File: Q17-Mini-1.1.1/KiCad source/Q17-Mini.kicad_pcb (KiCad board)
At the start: 2 copper layers, 95 x 75 mm, 88 parts, among them J1 Input, J2-1 SPK+, J2-2 SPK-, J3-1 V+, J3-2 GND, J3-3 V-, Q1 IRF610, Q10 KSA992, Q11 ZVP2106A, Q12 BD139, Q13 IRF610, Q14 IRF9610, Q15 FQA46N15, Q16 FQA36P15, Q2 KSA992, Q3 KSC1845, Q4 IRF9610, Q5 FQP3P20, Q6 FQP3N30, Q7 KSC1845, Q8 ZVN4206AV, Q9 ZVP2106A, U1 OPA1641, U1' OPA1641

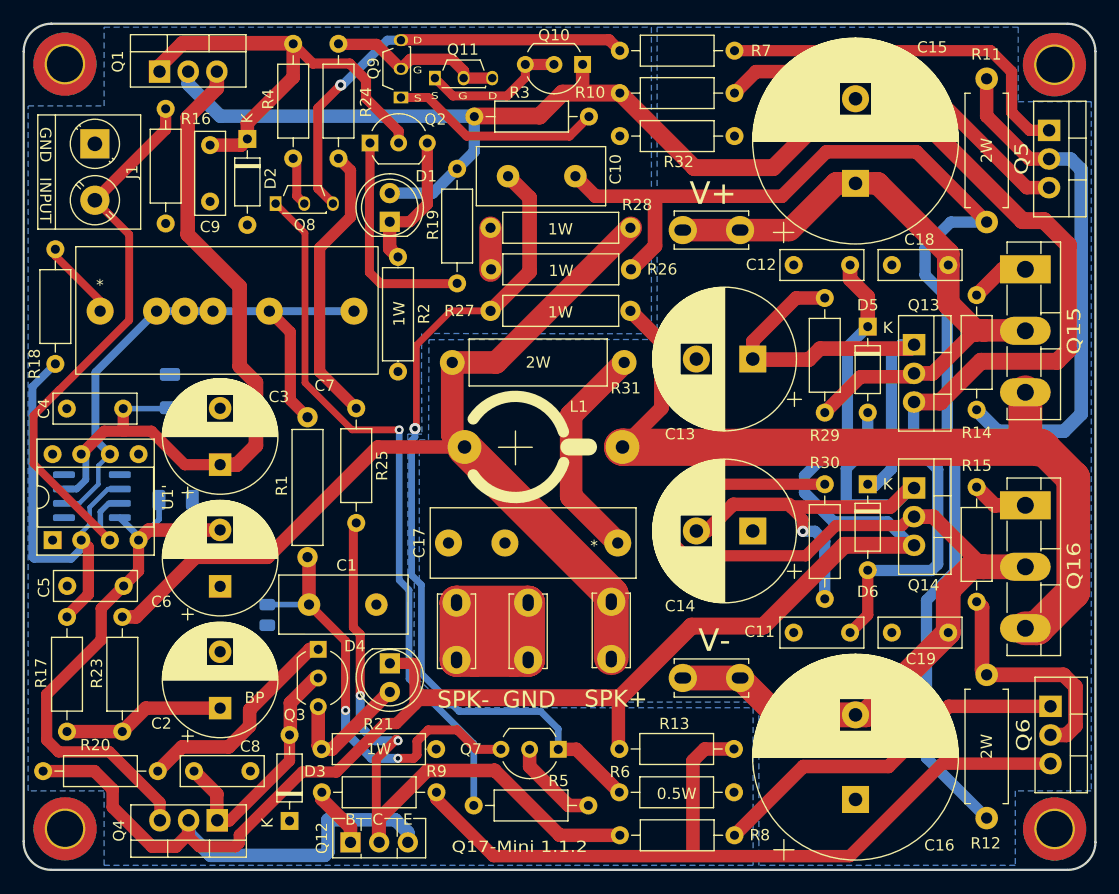
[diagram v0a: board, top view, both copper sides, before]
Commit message: Q17-Mini-1.1.2 release
- New vertical footprint for coil
- New SMD footprints on back PCB
- Update C7/R18 circuit position
- Some tracks optimisation
- New 3D and PCB pictures
- Archived version 1.1.1
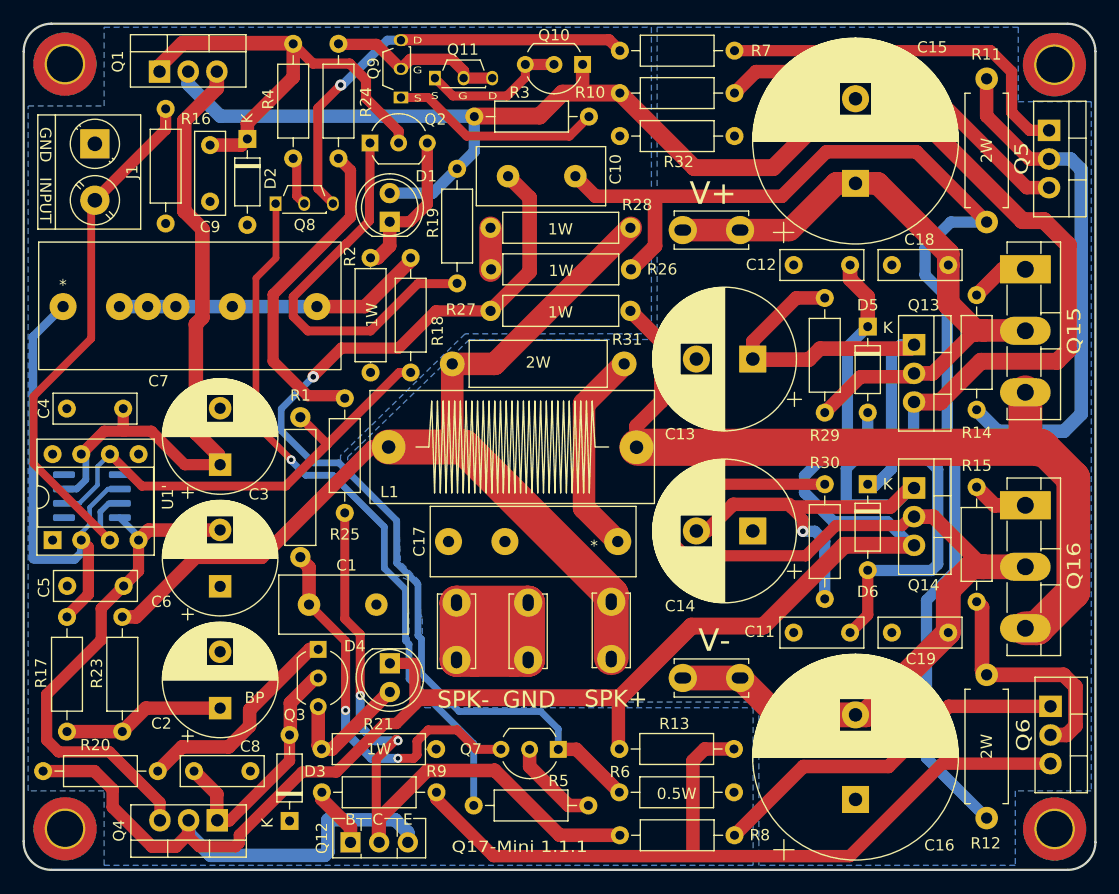
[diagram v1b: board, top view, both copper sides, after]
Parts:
- removed C4', C5': 100nF, Capacitor_SMD:C_1206_3216Metric
- removed R22: N.C, Resistor_SMD:R_0805_2012Metric
- C2: value 100uF/10V BP -> 100uF/16V BP
- L1: footprint Q17_Library:L_Axial_L22mm_D10mm_P21mm_vertical_Q17_Mini -> Inductor_THT:L_Axial_L22mm_D10mm_P21mm_Horizontal_Q17_Mini
- Q11, Q9: value ZVP2106A -> BS250P
- R17: value 7K32 -> 3k3
- R29, R30: value 100R -> 10R
- moved R18 32.9 mm to (134.1, 75.8), turned to -90 degrees
- moved L1 6.73 mm to (132.2, 92.6)
- moved C7 3.31 mm to (103.3, 80.1)
- moved R2 2.43 mm to (130.6, 75.8)
- moved R25 1.35 mm to (128.3, 88.3)
- moved R1 0.64 mm to (124.3, 89.9)
- moved C17 0.13 mm to (152.5, 101.0)
- moved R31 0.13 mm to (137.8, 85.2)
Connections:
- R1 pad 1: Net-(C7-Pad2) -> Net-(R1-Pad1)
- R17 pad 2: Net-(R17-Pad2) -> Net-(C7-Pad1)
- R18 pad 1: Net-(R17-Pad2) -> Net-(C7-Pad2)
- R18 pad 2: Net-(C7-Pad1) -> Net-(R1-Pad1)
- U1 pad 2: Net-(R17-Pad2) -> Net-(C7-Pad1)
- U1 pad 6: Net-(C7-Pad2) -> Net-(R1-Pad1)
- U1' pad 2: Net-(R17-Pad2) -> Net-(C7-Pad1)
- U1' pad 6: Net-(C7-Pad2) -> Net-(R1-Pad1)
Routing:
- net Net-(R1-Pad1): track 0.00 -> 42.2 mm
- net Net-(R17-Pad2): track 37.8 -> 0.00 mm
- net Net-(C7-Pad1): track 7.13 -> 43.4 mm
- net Net-(C7-Pad2): track 50.6 -> 27.7 mm
- net Net-(Q2-Pad1): track 19.7 -> 35.0 mm
- net Net-(C10-Pad2): track 74.6 -> 89.3 mm
- net Net-(C3-Pad1): track 65.4 -> 58.3 mm
- net Net-(C5-Pad2): track 49.3 -> 44.9 mm
- net Net-(R24-Pad2): track 25.1 -> 29.0 mm
- net Net-(J1-Pad2): track 53.3 -> 49.6 mm
- net Net-(C1-Pad1): track 37.8 -> 34.4 mm
- net Net-(L1-Pad2): track 75.7 -> 73.8 mm
- net Net-(C17-Pad1): track 19.7 -> 18.5 mm
- net Net-(Q12-Pad2): track 59.7 -> 60.8 mm
- net Net-(D1-Pad1): track 12.8 -> 13.7 mm
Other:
- board text added: "Q17-Mini 1.1.1"
- board text removed: "Q17-Mini 1.1.2"
